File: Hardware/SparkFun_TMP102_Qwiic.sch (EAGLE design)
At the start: 27 parts, among them J1 QWIIC, J2 QWIIC, J3 PTH, U1 TMP102

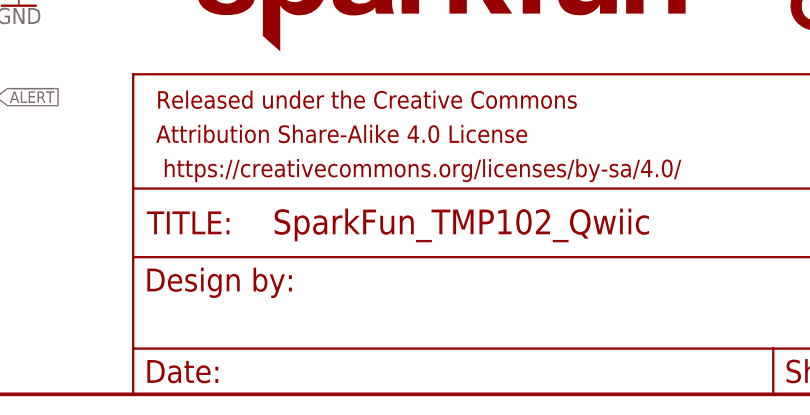
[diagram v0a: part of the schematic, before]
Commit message: v10 design review changes
- Added designer name to schematic
- Mitered I2C pull-up trances going to via
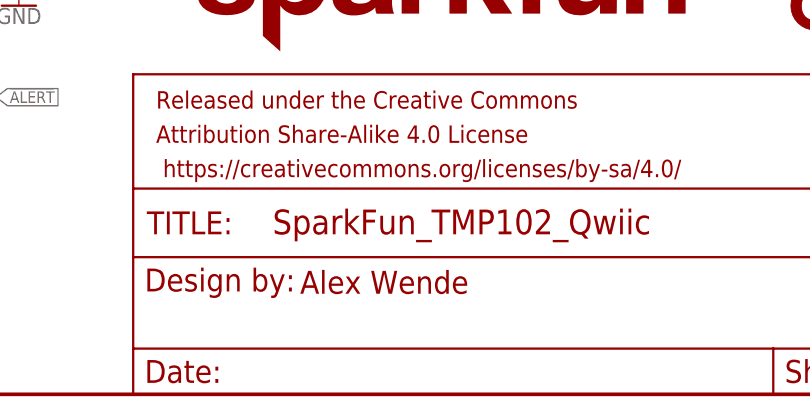
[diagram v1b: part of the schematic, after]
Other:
- note added: "Alex Wende"
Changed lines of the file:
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@@
 <wire x1="142.24" y1="185.42" x2="142.24" y2="81.28" width="0.2032" layer="97" style="shortdash"/>
 <wire x1="76.2" y1="81.28" x2="76.2" y2="0" width="0.2032" layer="97" style="shortdash"/>
+<text x="165.862" y="11.176" size="2.54" layer="94" font="vector">Alex Wende</text>
 </plain>
 <instances>
